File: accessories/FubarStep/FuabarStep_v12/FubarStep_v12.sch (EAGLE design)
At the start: 59 parts, among them IC2 SN754410NE, IC3 SN754410NE, U1 FUBARINO_SD, U2 FUBARINO_MINI, U3 OKI-78SR-5/1.5-W36H-C, X1 DC21MMX

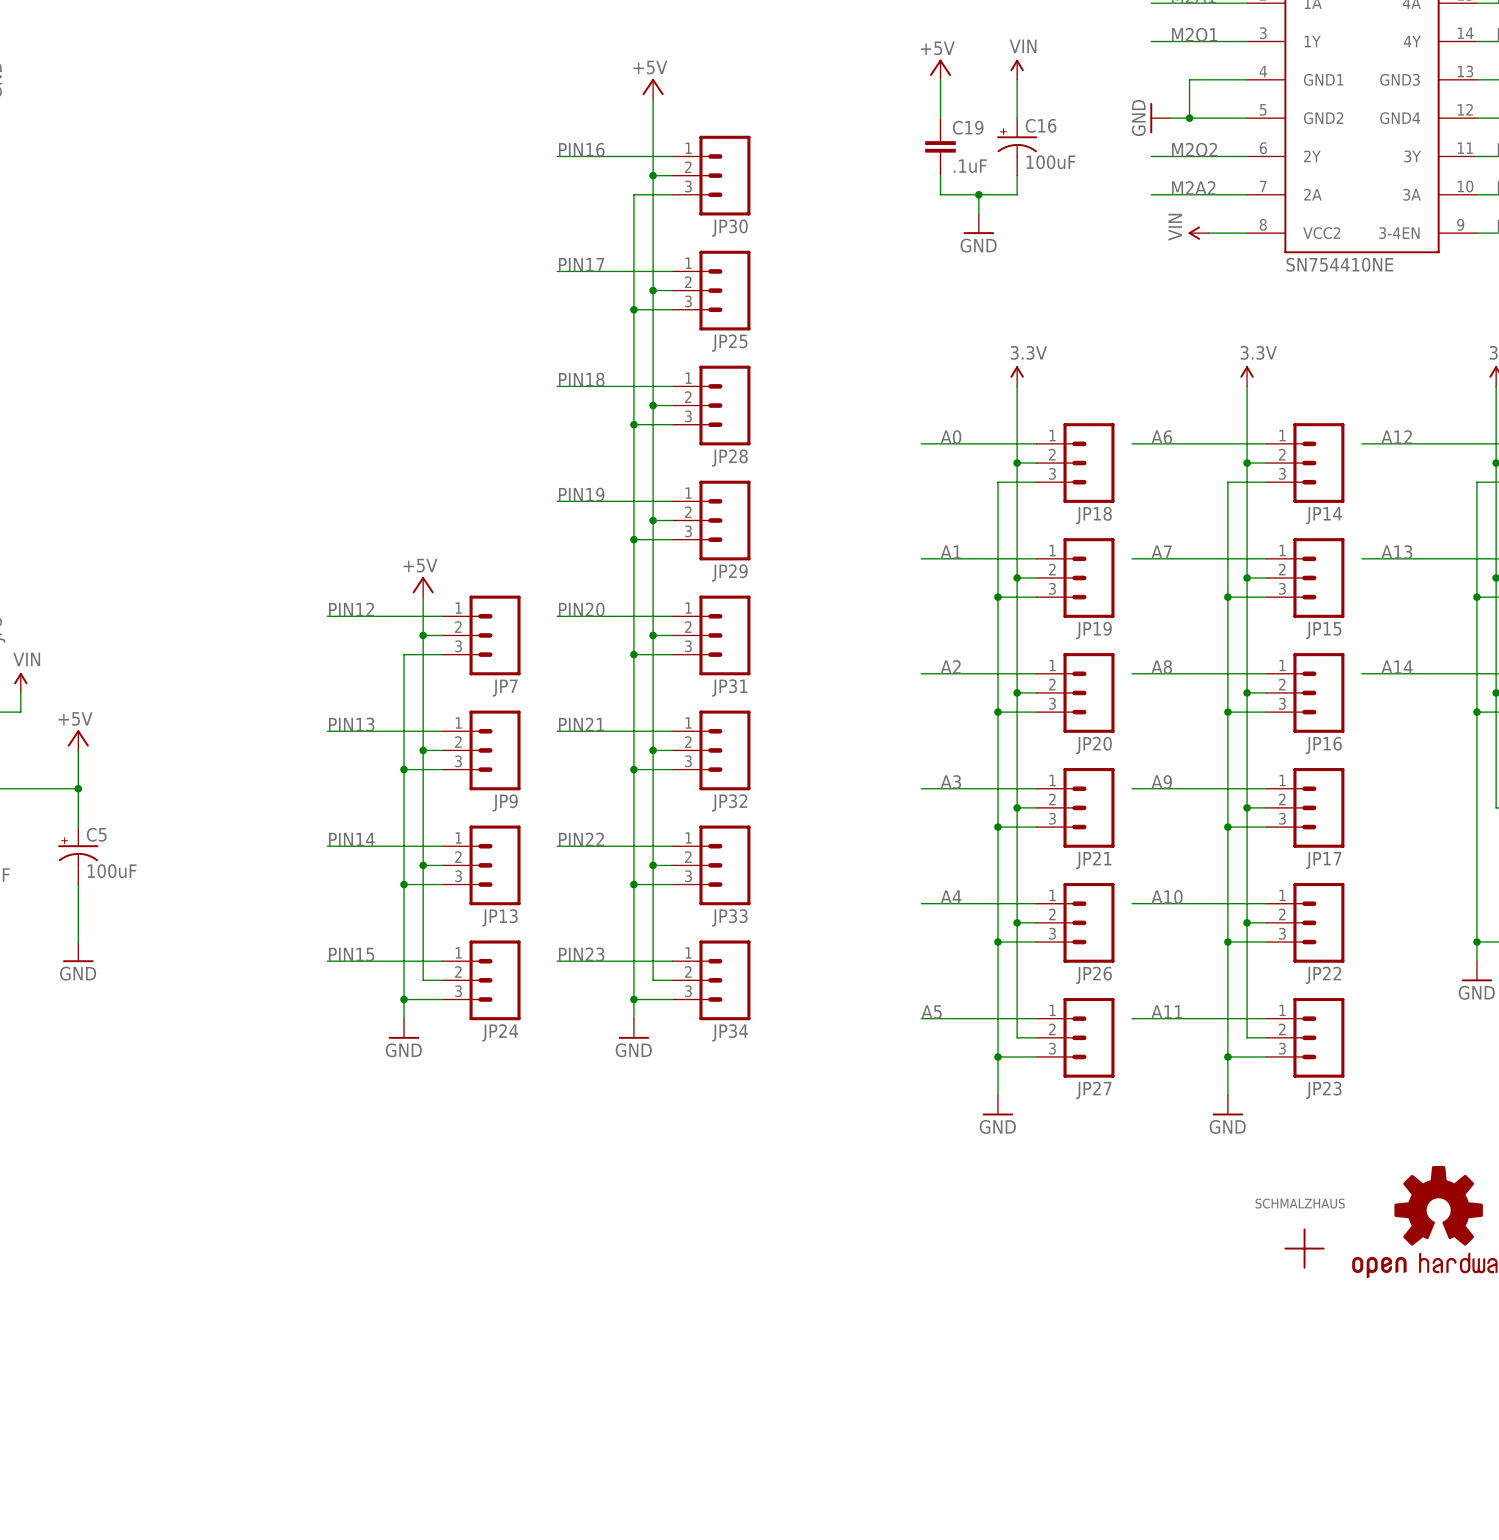
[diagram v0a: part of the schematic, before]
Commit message: Just playing with some ideas for v1.2 board - adding headers to every pin, for a complete break out board type feel.
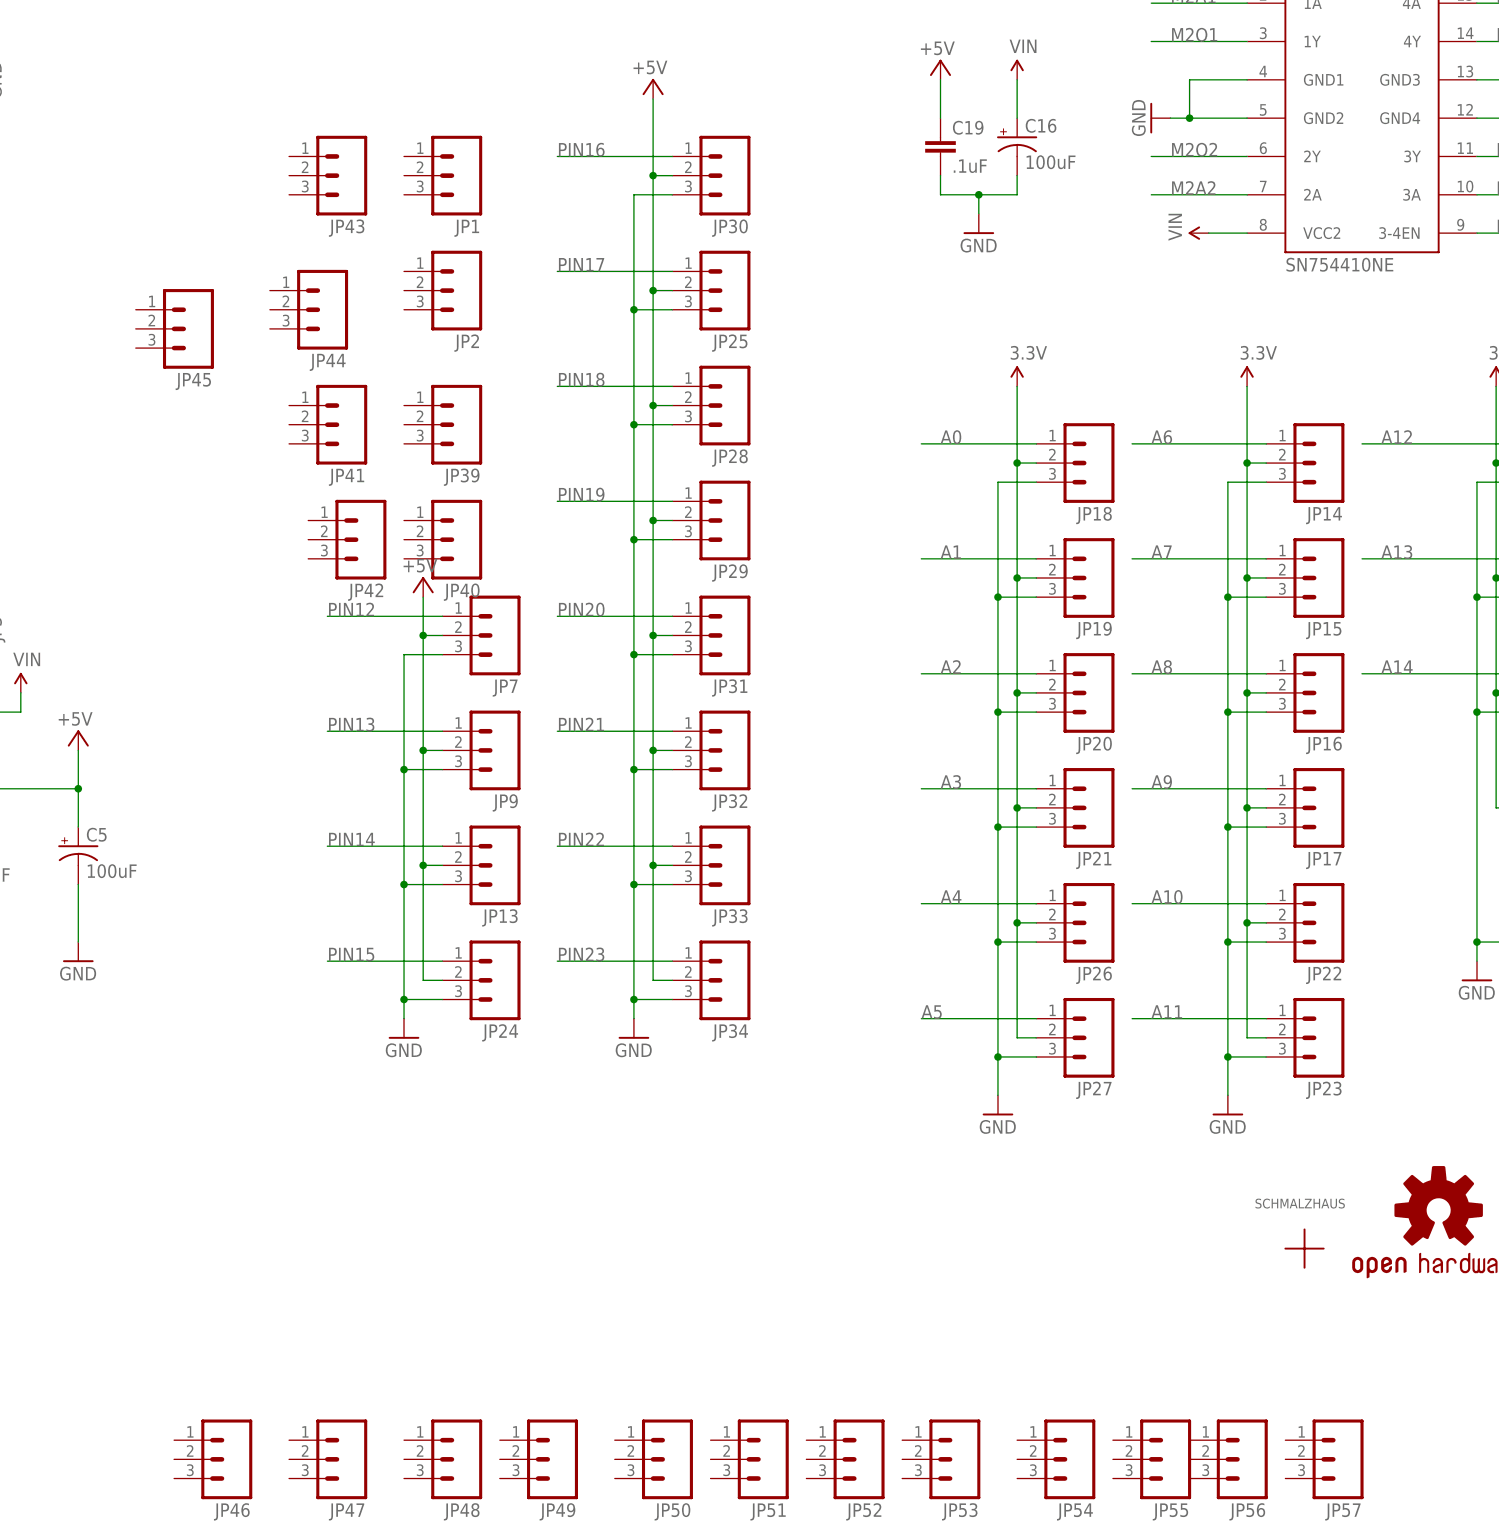
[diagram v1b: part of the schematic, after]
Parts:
- added JP1, JP2, JP39, JP40, JP41, JP42, JP43, JP44, JP45, JP46, JP47, JP48, JP49, JP50, JP51, JP52, JP53, JP54, JP55, JP56, JP57: (no value), SparkFun-Connectors:M03PTH
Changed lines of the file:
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@@
 <part name="GND10" library="supply1" deviceset="GND" device=""/>
 <part name="GND23" library="supply1" deviceset="GND" device=""/>
+<part name="JP1" library="SparkFun-Connectors" deviceset="M03" device="PTH"/>
+<part name="JP2" library="SparkFun-Connectors" deviceset="M03" device="PTH"/>
+<part name="JP39" library="SparkFun-Connectors" deviceset="M03" device="PTH"/>
+<part name="JP40" library="SparkFun-Connectors" deviceset="M03" device="PTH"/>
+<part name="JP41" library="SparkFun-Connectors" deviceset="M03" device="PTH"/>
+<part name="JP42" library="SparkFun-Connectors" deviceset="M03" device="PTH"/>
+<part name="JP43" library="SparkFun-Connectors" deviceset="M03" device="PTH"/>
+<part name="JP44" library="SparkFun-Connectors" deviceset="M03" device="PTH"/>
+<part name="JP45" library="SparkFun-Connectors" deviceset="M03" device="PTH"/>
+<part name="JP46" library="SparkFun-Connectors" deviceset="M03" device="PTH"/>
+<part name="JP47" library="SparkFun-Connectors" deviceset="M03" device="PTH"/>
+<part name="JP48" library="SparkFun-Connectors" deviceset="M03" device="PTH"/>
+<part name="JP49" library="SparkFun-Connectors" deviceset="M03" device="PTH"/>
+<part name="JP50" library="SparkFun-Connectors" deviceset="M03" device="PTH"/>
+<part name="JP51" library="SparkFun-Connectors" deviceset="M03" device="PTH"/>
+<part name="JP52" library="SparkFun-Connectors" deviceset="M03" device="PTH"/>
+<part name="JP53" library="SparkFun-Connectors" deviceset="M03" device="PTH"/>
+<part name="JP54" library="SparkFun-Connectors" deviceset="M03" device="PTH"/>
+<part name="JP55" library="SparkFun-Connectors" deviceset="M03" device="PTH"/>
+<part name="JP56" library="SparkFun-Connectors" deviceset="M03" device="PTH"/>
+<part name="JP57" library="SparkFun-Connectors" deviceset="M03" device="PTH"/>
 </parts>
 <sheets>
@@
 <instance part="GND10" gate="1" x="342.9" y="213.36"/>
 <instance part="GND23" gate="1" x="342.9" y="170.18"/>
+<instance part="JP1" gate="G$1" x="142.24" y="152.4" rot="R180"/>
+<instance part="JP2" gate="G$1" x="142.24" y="137.16" rot="R180"/>
+<instance part="JP39" gate="G$1" x="142.24" y="119.38" rot="R180"/>
+<instance part="JP40" gate="G$1" x="142.24" y="104.14" rot="R180"/>
+<instance part="JP41" gate="G$1" x="127" y="119.38" rot="R180"/>
+<instance part="JP42" gate="G$1" x="129.54" y="104.14" rot="R180"/>
+<instance part="JP43" gate="G$1" x="127" y="152.4" rot="R180"/>
+<instance part="JP44" gate="G$1" x="124.46" y="134.62" rot="R180"/>
+<instance part="JP45" gate="G$1" x="106.68" y="132.08" rot="R180"/>
+<instance part="JP46" gate="G$1" x="111.76" y="-17.78" rot="R180"/>
+<instance part="JP47" gate="G$1" x="127" y="-17.78" rot="R180"/>
+<instance part="JP48" gate="G$1" x="142.24" y="-17.78" rot="R180"/>
+<instance part="JP49" gate="G$1" x="154.94" y="-17.78" rot="R180"/>
+<instance part="JP50" gate="G$1" x="170.18" y="-17.78" rot="R180"/>
+<instance part="JP51" gate="G$1" x="182.88" y="-17.78" rot="R180"/>
+<instance part="JP52" gate="G$1" x="195.58" y="-17.78" rot="R180"/>
+<instance part="JP53" gate="G$1" x="208.28" y="-17.78" rot="R180"/>
+<instance part="JP54" gate="G$1" x="223.52" y="-17.78" rot="R180"/>
+<instance part="JP55" gate="G$1" x="236.22" y="-17.78" rot="R180"/>
+<instance part="JP56" gate="G$1" x="246.38" y="-17.78" rot="R180"/>
+<instance part="JP57" gate="G$1" x="259.08" y="-17.78" rot="R180"/>
 </instances>
 <busses>

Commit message: New version of FubarStep - almost ready to go.
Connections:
- removed net +3V3: U1.3.3V@2
- new net PIN24: JP42.1, U1.PIN24/SCK
- new net PIN25: JP41.1, U1.PIN25/SDI
- new net PIN26: JP40.1, U1.PIN26/SDO
- new net PIN27: JP39.1, U1.PIN27/SS
- net +5V: now also JP46.2, JP47.2, JP48.2, JP49.2, JP50.2, JP51.2, JP52.2, JP53.2, JP54.2, JP55.2, JP56.2, JP57.2
- net 3.3V: now also JP1.2, JP2.2, JP39.2, JP40.2, JP41.2, JP42.2, JP43.2, JP44.1, JP44.2, JP45.2, U1.3.3V@2
- net GND: now also JP1.3, JP2.3, JP39.3, JP40.3, JP41.3, JP42.3, JP43.1, JP43.3, JP44.3, JP45.3, JP46.3, JP47.3, JP48.3, JP49.3, JP50.3, JP51.3, JP52.3, JP53.3, JP54.3, JP55.3, JP56.3, JP57.3
- net M1A1: now also JP55.1
- net M1A2: now also JP57.1
- net M1A3: now also JP56.1
- net M1A4: now also JP54.1
- net M1EN12: now also JP50.1
- net M1EN34: now also JP49.1
- net M2A1: now also JP52.1
- net M2A2: now also JP51.1
- net M2A3: now also JP46.1
- net M2A4: now also JP53.1
- net M2EN12: now also JP48.1
- net M2EN34: now also JP47.1
- net RESET: now also JP45.1
- net RX: now also JP1.1
- net TX: now also JP2.1
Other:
- note added: "RC Servo/5V tolerant GPIO"
- note removed: "RC Servo/5V tollerant GPIO"
- moved on the sheet: C3, JP1, JP10, JP11, JP12, JP13, JP14, JP15, JP16, JP17, JP18, JP19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

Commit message: Sent these boards off to Seeed for production.
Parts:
- removed C16, C17, C5: 100uF, SparkFun-Capacitors:CAP_POLPTH1
- added C2, C4, C6: 100uF, SchmalzHaus:CAP_ELECTROLYTICPTH1_BPS
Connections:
- net +5V: now also C2.+; no longer C5.+
- net GND: now also C2.-, C4.-, C6.-; no longer C16.-, C17.-, C5.-
- net VIN: now also C4.+, C6.+; no longer C16.+, C17.+
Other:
- note added: "6V-12V DC or 5V DC in"
- note added: "Power Select JumperJP3 1-2 = 6V-12V in, use regulator 2-3 = 5V in, bypass regulator"
- note added: "v1.2 : 11/03/2013 Fixed Fubarino Mini TX/RX swap on FTDI connector Connected all Fubarino SD and Mini I/O pins to headers Changed 100uF cap footprint slightly Moved things around for easier assembly"
- note removed: "12V DC or 5V DC in"
- note removed: "Power Select Jumper 1-2 = 12V in, use regulator 2-3 = 5V in, bypass regulator"
- note removed: "v1.2 : Fixed Fubarino Mini TX/RX swap on FTDI connector"
- moved on the sheet: C1, C10, C11, C12, C13, C14, C15, C18, C19, C3, C8, C9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
